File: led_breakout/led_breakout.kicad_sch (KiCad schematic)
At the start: 19 parts, among them J1 S-, J2 P, J3 P, J4 S+

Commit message: Edit Schematic and add Parts Number
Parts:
- D1: Link (none) -> https://www.digikey.ch/en/products/detail/seoul-semiconduct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; SPN (none) -> 897-1393-1-ND; Supplier (none) -> Digikey
- J1, J3: Link (none) -> https://www.digikey.ch/fr/products/detail/sullins-connector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; SPN (none) -> S5438-ND; Supplier (none) -> Digikey
- J2, J4: Link (none) -> https://www.digikey.ch/fr/products/detail/molex/0901210122/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; SPN (none) -> WM8096-ND; Supplier (none) -> Digikey
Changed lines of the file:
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@@
+      (effects (font (size 1.27 1.27)) hide)
+    )
+    (property "Link" "https://www.digikey.ch/fr/products/detail/sullins-connector-solutions/PPTC021LGBN-RC/775896" (id 4) (at 162.56 114.3 0)
+      (effects (font (size 1.27 1.27)) hide)
+    )
+    (property "SPN" "S5438-ND" (id 5) (at 162.56 114.3 0)
+      (effects (font (size 1.27 1.27)) hide)
+    )
+    (property "Supplier" "Digikey" (id 6) (at 162.56 114.3 0)
       (effects (font (size 1.27 1.27)) hide)
     )
@@
       (effects (font (size 1.27 1.27)) hide)
     )
+    (property "Link" "https://www.digikey.ch/fr/products/detail/sullins-connector-solutions/PPTC021LGBN-RC/775896" (id 4) (at 140.97 96.52 0)
+      (effects (font (size 1.27 1.27)) hide)
+    )
+    (property "SPN" "S5438-ND" (id 5) (at 140.97 96.52 0)
+      (effects (font (size 1.27 1.27)) hide)
+    )
+    (property "Supplier" "Digikey" (id 6) (at 140.97 96.52 0)
+      (effects (font (size 1.27 1.27)) hide)
+    )
     (pin "1")
     (pin "2")
@@
       (effects (font (size 1.27 1.27)) hide)
     )
+    (property "Link" "https://www.digikey.ch/en/products/detail/seoul-semiconductor-inc/S1S0-3030509506-0000003S-00001/9997428" (id 4) (at 163.83 95.25 0)
+      (effects (font (size 1.27 1.27)) hide)
+    )
+    (property "SPN" "897-1393-1-ND" (id 5) (at 163.83 95.25 0)
+      (effects (font (size 1.27 1.27)) hide)
+    )
+    (property "Supplier" "Digikey" (id 6) (at 163.83 95.25 0)
+      (effects (font (size 1.27 1.27)) hide)
+    )
     (pin "1")
     (pin "2")
@@
       (effects (font (size 1.27 1.27)) hide)
     )
+    (property "Link" "https://www.digikey.ch/fr/products/detail/molex/0901210122/760811?s=N4IgTCBcDaIJwAYCMYkFpljAAgLYHsAbAUwA8QBdAXyA" (id 4) (at 162.56 63.5 0)
+      (effects (font (size 1.27 1.27)) hide)
+    )
+    (property "SPN" "WM8096-ND" (id 5) (at 162.56 63.5 0)
+      (effects (font (size 1.27 1.27)) hide)
+    )
+    (property "Supplier" "Digikey" (id 6) (at 162.56 63.5 0)
+      (effects (font (size 1.27 1.27)) hide)
+    )
     (pin "1")
     (pin "2")
@@
       (effects (font (size 1.27 1.27)) hide)
     )
+    (property "Link" "https://www.digikey.ch/fr/products/detail/molex/0901210122/760811?s=N4IgTCBcDaIJwAYCMYkFpljAAgLYHsAbAUwA8QBdAXyA" (id 4) (at 198.12 96.52 0)
+      (effects (font (size 1.27 1.27)) hide)
+    )
+    (property "SPN" "WM8096-ND" (id 5) (at 198.12 96.52 0)
+      (effects (font (size 1.27 1.27)) hide)
+    )
+    (property "Supplier" "Digikey" (id 6) (at 198.12 96.52 0)
+      (effects (font (size 1.27 1.27)) hide)
+    )

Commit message: update resistor value
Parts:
- R1: value R -> 100
- R2, R3: value R -> np
- R4: value R -> 0
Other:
- note added: "multiple footprint"
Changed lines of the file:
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@@
     (stroke (width 0) (type default) (color 0 0 0 0))
+  )
+  (text "multiple footprint" (at 139.7 83.82 0)
+    (effects (font (size 1.27 1.27)) (justify left bottom))
   )
   (label "VCC" (at 181.61 99.06 0)
@@
     (in_bom yes) (on_board yes)
     (property "Reference" "R2" (id 0) (at 177.8 92.71 90))
-    (property "Value" "R" (id 1) (at 171.45 92.71 90))
+    (property "Value" "np" (id 1) (at 171.45 92.71 90))
     (property "Footprint" "Resistor_SMD:R_2512_6332Metric" (id 2) (at 175.26 97.028 90)
       (effects (font (size 1.27 1.27)) hide)
@@
     (in_bom yes) (on_board yes)
     (property "Reference" "R1" (id 0) (at 166.37 86.36 90))
-    (property "Value" "R" (id 1) (at 161.29 86.36 90))
+    (property "Value" "100" (id 1) (at 161.29 86.36 90))
     (property "Footprint" "Resistor_SMD:R_2512_6332Metric" (id 2) (at 163.83 90.678 90)
       (effects (font (size 1.27 1.27)) hide)
@@
     (in_bom yes) (on_board yes)
     (property "Reference" "R4" (id 0) (at 179.07 86.36 90))
-    (property "Value" "R" (id 1) (at 171.45 86.36 90))
+    (property "Value" "0" (id 1) (at 171.45 86.36 90))
     (property "Footprint" "Resistor_SMD:R_0805_2012Metric" (id 2) (at 175.26 90.678 90)
       (effects (font (size 1.27 1.27)) hide)
@@
     (in_bom yes) (on_board yes)
     (property "Reference" "R3" (id 0) (at 166.37 81.28 90))
-    (property "Value" "R" (id 1) (at 161.29 81.28 90))
+    (property "Value" "np" (id 1) (at 161.29 81.28 90))
     (property "Footprint" "Resistor_SMD:R_0805_2012Metric" (id 2) (at 163.83 85.598 90)
       (effects (font (size 1.27 1.27)) hide)
@@
     )
     (path "/888059b3-2471-43ee-a2b4-3fd09f693b37"
-      (reference "R1") (unit 1) (value "R") (footprint "Resistor_SMD:R_2512_6332Metric")
+      (reference "R1") (unit 1) (value "100") (footprint "Resistor_SMD:R_2512_6332Metric")
     )
     (path "/2102c637-9f11-48f1-aae6-b4139dc22be2"
-      (reference "R2") (unit 1) (value "R") (footprint "Resistor_SMD:R_2512_6332Metric")
+      (reference "R2") (unit 1) (value "np") (footprint "Resistor_SMD:R_2512_6332Metric")
     )
     (path "/e8582bb9-de0c-4720-baed-24965142a913"
-      (reference "R3") (unit 1) (value "R") (footprint "Resistor_SMD:R_0805_2012Metric")
+      (reference "R3") (unit 1) (value "np") (footprint "Resistor_SMD:R_0805_2012Metric")
     )
     (path "/a7ad0f99-35cc-44ad-b8a5-2ca7a8c56836"
-      (reference "R4") (unit 1) (value "R") (footprint "Resistor_SMD:R_0805_2012Metric")
-    )
-  )
+      (reference "R4") (unit 1) (value "0") (footprint "Resistor_SMD:R_0805_2012Metric")
+    )
+  )

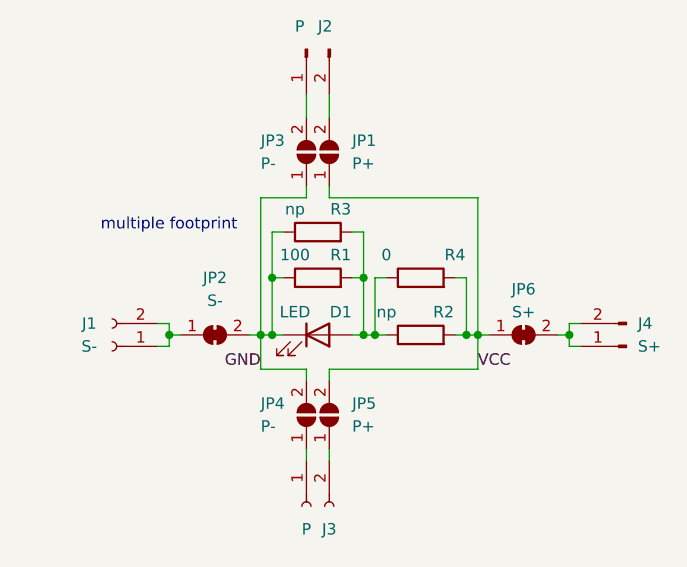
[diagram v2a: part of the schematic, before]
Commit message: Fix PCB errors after first assembly
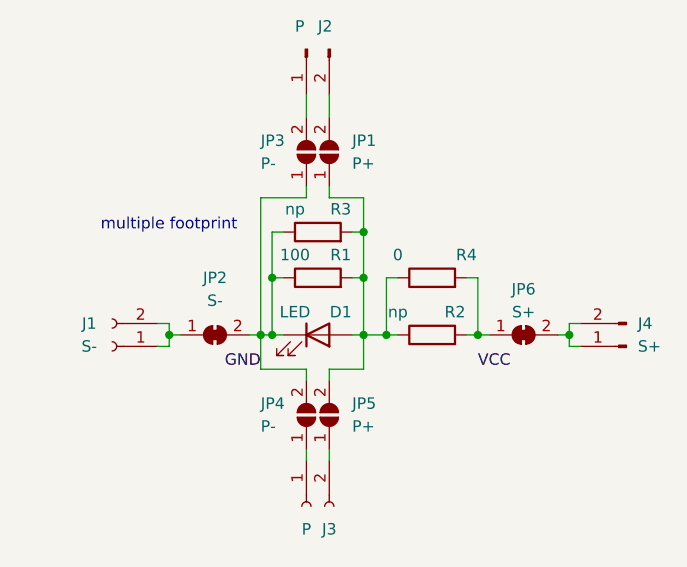
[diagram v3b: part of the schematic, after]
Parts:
- D1: footprint LED_SMD:LED_1210_3225Metric_Pad1.42x2.65mm_HandSolder -> LED_SMD:LED_Cree-XH
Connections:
- net VCC: no longer JP1.1 (A), JP5.2 (B), JP6.1 (A), R2.2, R4.2
- net at D1.2 (A), R1.2, R2.1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: now also JP1.1 (A), JP5.2 (B)
- new net: JP6.1 (A), R2.2, R4.2
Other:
- moved on the sheet: R2, R4
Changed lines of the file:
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@@
   (junction (at 157.48 95.25) (diameter 0) (color 0 0 0 0)
   )
+  (junction (at 168.91 83.82) (diameter 0) (color 0 0 0 0)
+  )
   (junction (at 168.91 88.9) (diameter 0) (color 0 0 0 0)
   )
   (junction (at 158.75 88.9) (diameter 0) (color 0 0 0 0)
   )
+  (junction (at 191.77 95.25) (diameter 0) (color 0 0 0 0)
+  )
+  (junction (at 147.32 95.25) (diameter 0) (color 0 0 0 0)
+  )
   (junction (at 181.61 95.25) (diameter 0) (color 0 0 0 0)
   )
-  (junction (at 191.77 95.25) (diameter 0) (color 0 0 0 0)
-  )
-  (junction (at 147.32 95.25) (diameter 0) (color 0 0 0 0)
-  )
-  (junction (at 180.34 95.25) (diameter 0) (color 0 0 0 0)
-  )
-  (junction (at 170.18 95.25) (diameter 0) (color 0 0 0 0)
+  (junction (at 171.45 95.25) (diameter 0) (color 0 0 0 0)
   )
   (junction (at 168.91 95.25) (diameter 0) (color 0 0 0 0)
@@
   (junction (at 158.75 95.25) (diameter 0) (color 0 0 0 0)
   )
-  (wire (pts (xy 170.18 88.9) (xy 171.45 88.9))
+  (wire (pts (xy 171.45 88.9) (xy 172.72 88.9))
     (stroke (width 0) (type default) (color 0 0 0 0))
   )
@@
     (stroke (width 0) (type default) (color 0 0 0 0))
   )
-  (wire (pts (xy 170.18 95.25) (xy 171.45 95.25))
+  (wire (pts (xy 171.45 95.25) (xy 172.72 95.25))
     (stroke (width 0) (type default) (color 0 0 0 0))
   )
@@
     (stroke (width 0) (type default) (color 0 0 0 0))
   )
-  (wire (pts (xy 180.34 88.9) (xy 180.34 95.25))
+  (wire (pts (xy 181.61 88.9) (xy 181.61 95.25))
     (stroke (width 0) (type default) (color 0 0 0 0))
   )
@@
     (stroke (width 0) (type default) (color 0 0 0 0))
   )
-  (wire (pts (xy 179.07 88.9) (xy 180.34 88.9))
-    (stroke (width 0) (type default) (color 0 0 0 0))
-  )
-  (wire (pts (xy 168.91 95.25) (xy 170.18 95.25))
+  (wire (pts (xy 180.34 88.9) (xy 181.61 88.9))
     (stroke (width 0) (type default) (color 0 0 0 0))
   )
@@
     (stroke (width 0) (type default) (color 0 0 0 0))
   )
+  (wire (pts (xy 168.91 80.01) (xy 168.91 83.82))
+    (stroke (width 0) (type default) (color 0 0 0 0))
+  )
+  (wire (pts (xy 191.77 93.98) (xy 193.04 93.98))
+    (stroke (width 0) (type default) (color 0 0 0 0))
+  )
+  (wire (pts (xy 165.1 80.01) (xy 168.91 80.01))
+    (stroke (width 0) (type default) (color 0 0 0 0))
+  )
+  (wire (pts (xy 147.32 95.25) (xy 148.59 95.25))
+    (stroke (width 0) (type default) (color 0 0 0 0))
+  )
+  (wire (pts (xy 146.05 96.52) (xy 147.32 96.52))
+    (stroke (width 0) (type default) (color 0 0 0 0))
+  )
+  (wire (pts (xy 167.64 95.25) (xy 168.91 95.25))
+    (stroke (width 0) (type default) (color 0 0 0 0))
+  )
+  (wire (pts (xy 167.64 83.82) (xy 168.91 83.82))
+    (stroke (width 0) (type default) (color 0 0 0 0))
+  )
+  (wire (pts (xy 160.02 88.9) (xy 158.75 88.9))
+    (stroke (width 0) (type default) (color 0 0 0 0))
+  )
+  (wire (pts (xy 180.34 95.25) (xy 181.61 95.25))
+    (stroke (width 0) (type default) (color 0 0 0 0))
+  )
+  (wire (pts (xy 168.91 95.25) (xy 171.45 95.25))
+    (stroke (width 0) (type default) (color 0 0 0 0))
+  )
+  (wire (pts (xy 171.45 88.9) (xy 171.45 95.25))
+    (stroke (width 0) (type default) (color 0 0 0 0))
+  )
+  (wire (pts (xy 162.56 68.58) (xy 162.56 71.12))
+    (stroke (width 0) (type default) (color 0 0 0 0))
+  )
+  (wire (pts (xy 162.56 99.06) (xy 162.56 100.33))
+    (stroke (width 0) (type default) (color 0 0 0 0))
+  )
+  (wire (pts (xy 165.1 107.95) (xy 165.1 109.22))
+    (stroke (width 0) (type default) (color 0 0 0 0))
+  )
+  (wire (pts (xy 165.1 68.58) (xy 165.1 71.12))
+    (stroke (width 0) (type default) (color 0 0 0 0))
+  )
+  (wire (pts (xy 147.32 95.25) (xy 147.32 93.98))
+    (stroke (width 0) (type default) (color 0 0 0 0))
+  )
+  (wire (pts (xy 165.1 99.06) (xy 168.91 99.06))
+    (stroke (width 0) (type default) (color 0 0 0 0))
+  )
+  (wire (pts (xy 156.21 95.25) (xy 157.48 95.25))
+    (stroke (width 0) (type default) (color 0 0 0 0))
+  )
+  (wire (pts (xy 168.91 95.25) (xy 168.91 88.9))
+    (stroke (width 0) (type default) (color 0 0 0 0))
+  )
+  (wire (pts (xy 191.77 96.52) (xy 191.77 95.25))
+    (stroke (width 0) (type default) (color 0 0 0 0))
+  )
+  (wire (pts (xy 158.75 88.9) (xy 158.75 95.25))
+    (stroke (width 0) (type default) (color 0 0 0 0))
+  )
+  (wire (pts (xy 162.56 80.01) (xy 157.48 80.01))
+    (stroke (width 0) (type default) (color 0 0 0 0))
+  )
   (wire (pts (xy 181.61 95.25) (xy 182.88 95.25))
     (stroke (width 0) (type default) (color 0 0 0 0))
   )
-  (wire (pts (xy 191.77 93.98) (xy 193.04 93.98))
-    (stroke (width 0) (type default) (color 0 0 0 0))
-  )
-  (wire (pts (xy 181.61 80.01) (xy 181.61 95.25))
-    (stroke (width 0) (type default) (color 0 0 0 0))
-  )
-  (wire (pts (xy 165.1 80.01) (xy 181.61 80.01))
-    (stroke (width 0) (type default) (color 0 0 0 0))
-  )
-  (wire (pts (xy 147.32 95.25) (xy 148.59 95.25))
-    (stroke (width 0) (type default) (color 0 0 0 0))
-  )
-  (wire (pts (xy 146.05 96.52) (xy 147.32 96.52))
-    (stroke (width 0) (type default) (color 0 0 0 0))
-  )
-  (wire (pts (xy 167.64 95.25) (xy 168.91 95.25))
-    (stroke (width 0) (type default) (color 0 0 0 0))
-  )
-  (wire (pts (xy 167.64 83.82) (xy 168.91 83.82))
-    (stroke (width 0) (type default) (color 0 0 0 0))
-  )
-  (wire (pts (xy 160.02 88.9) (xy 158.75 88.9))
-    (stroke (width 0) (type default) (color 0 0 0 0))
-  )
-  (wire (pts (xy 179.07 95.25) (xy 180.34 95.25))
-    (stroke (width 0) (type default) (color 0 0 0 0))
-  )
-  (wire (pts (xy 165.1 99.06) (xy 181.61 99.06))
-    (stroke (width 0) (type default) (color 0 0 0 0))
-  )
-  (wire (pts (xy 170.18 88.9) (xy 170.18 95.25))
-    (stroke (width 0) (type default) (color 0 0 0 0))
-  )
-  (wire (pts (xy 162.56 68.58) (xy 162.56 71.12))
-    (stroke (width 0) (type default) (color 0 0 0 0))
-  )
-  (wire (pts (xy 162.56 99.06) (xy 162.56 100.33))
-    (stroke (width 0) (type default) (color 0 0 0 0))
-  )
-  (wire (pts (xy 165.1 107.95) (xy 165.1 109.22))
-    (stroke (width 0) (type default) (color 0 0 0 0))
-  )
-  (wire (pts (xy 181.61 99.06) (xy 181.61 95.25))
-    (stroke (width 0) (type default) (color 0 0 0 0))
-  )
-  (wire (pts (xy 165.1 68.58) (xy 165.1 71.12))
-    (stroke (width 0) (type default) (color 0 0 0 0))
-  )
-  (wire (pts (xy 147.32 95.25) (xy 147.32 93.98))
-    (stroke (width 0) (type default) (color 0 0 0 0))
-  )
-  (wire (pts (xy 156.21 95.25) (xy 157.48 95.25))
-    (stroke (width 0) (type default) (color 0 0 0 0))
-  )
-  (wire (pts (xy 168.91 95.25) (xy 168.91 88.9))
-    (stroke (width 0) (type default) (color 0 0 0 0))
-  )
-  (wire (pts (xy 191.77 96.52) (xy 191.77 95.25))
-    (stroke (width 0) (type default) (color 0 0 0 0))
-  )
-  (wire (pts (xy 158.75 88.9) (xy 158.75 95.25))
-    (stroke (width 0) (type default) (color 0 0 0 0))
-  )
-  (wire (pts (xy 162.56 80.01) (xy 157.48 80.01))
-    (stroke (width 0) (type default) (color 0 0 0 0))
-  )
-  (wire (pts (xy 180.34 95.25) (xy 181.61 95.25))
-    (stroke (width 0) (type default) (color 0 0 0 0))
-  )
   (wire (pts (xy 157.48 99.06) (xy 162.56 99.06))
+    (stroke (width 0) (type default) (color 0 0 0 0))
+  )
+  (wire (pts (xy 168.91 99.06) (xy 168.91 95.25))
     (stroke (width 0) (type default) (color 0 0 0 0))
   )
@@
     (pin "2")
   )
-  (symbol (lib_id "Device:R") (at 175.26 95.25 90) (unit 1)
-    (in_bom yes) (on_board yes)
-    (property "Reference" "R2" (id 0) (at 177.8 92.71 90))
-    (property "Value" "np" (id 1) (at 171.45 92.71 90))
-    (property "Footprint" "Resistor_SMD:R_2512_6332Metric" (id 2) (at 175.26 97.028 90)
-      (effects (font (size 1.27 1.27)) hide)
-    )
-    (property "Datasheet" "~" (id 3) (at 175.26 95.25 0)
+  (symbol (lib_id "Device:R") (at 176.53 95.25 90) (unit 1)
+    (in_bom yes) (on_board yes)
+    (property "Reference" "R2" (id 0) (at 179.07 92.71 90))
+    (property "Value" "np" (id 1) (at 172.72 92.71 90))
+    (property "Footprint" "Resistor_SMD:R_2512_6332Metric" (id 2) (at 176.53 97.028 90)
+      (effects (font (size 1.27 1.27)) hide)
+    )
+    (property "Datasheet" "~" (id 3) (at 176.53 95.25 0)
       (effects (font (size 1.27 1.27)) hide)
     )
@@
     (pin "2")
   )
-  (symbol (lib_id "Device:R") (at 175.26 88.9 90) (unit 1)
-    (in_bom yes) (on_board yes)
-    (property "Reference" "R4" (id 0) (at 179.07 86.36 90))
-    (property "Value" "0" (id 1) (at 171.45 86.36 90))
-    (property "Footprint" "Resistor_SMD:R_0805_2012Metric" (id 2) (at 175.26 90.678 90)
-      (effects (font (size 1.27 1.27)) hide)
-    )
-    (property "Datasheet" "~" (id 3) (at 175.26 88.9 0)
+  (symbol (lib_id "Device:R") (at 176.53 88.9 90) (unit 1)
+    (in_bom yes) (on_board yes)
+    (property "Reference" "R4" (id 0) (at 180.34 86.36 90))
+    (property "Value" "0" (id 1) (at 172.72 86.36 90))
+    (property "Footprint" "Resistor_SMD:R_0805_2012Metric" (id 2) (at 176.53 90.678 90)
+      (effects (font (size 1.27 1.27)) hide)
+    )
+    (property "Datasheet" "~" (id 3) (at 176.53 88.9 0)
       (effects (font (size 1.27 1.27)) hide)
     )
@@
     (property "Reference" "D1" (id 0) (at 166.37 92.71 0))
     (property "Value" "LED" (id 1) (at 161.29 92.71 0))
-    (property "Footprint" "LED_SMD:LED_1210_3225Metric_Pad1.42x2.65mm_HandSolder" (id 2) (at 163.83 95.25 0)
+    (property "Footprint" "LED_SMD:LED_Cree-XH" (id 2) (at 163.83 95.25 0)
       (effects (font (size 1.27 1.27)) hide)
     )
@@
   (symbol_instances
     (path "/c9ed9b4d-6b20-4fe2-a899-d5d88cee8937"
-      (reference "D1") (unit 1) (value "LED") (footprint "LED_SMD:LED_1210_3225Metric_Pad1.42x2.65mm_HandSolder")
+      (reference "D1") (unit 1) (value "LED") (footprint "LED_SMD:LED_Cree-XH")
     )
     (path "/b34a6863-f7b1-45f9-be7e-3465e3207905"
